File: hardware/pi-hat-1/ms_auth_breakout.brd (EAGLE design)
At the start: 66.8 x 29.2 mm, 20 parts, among them IC1 ULN2003AD

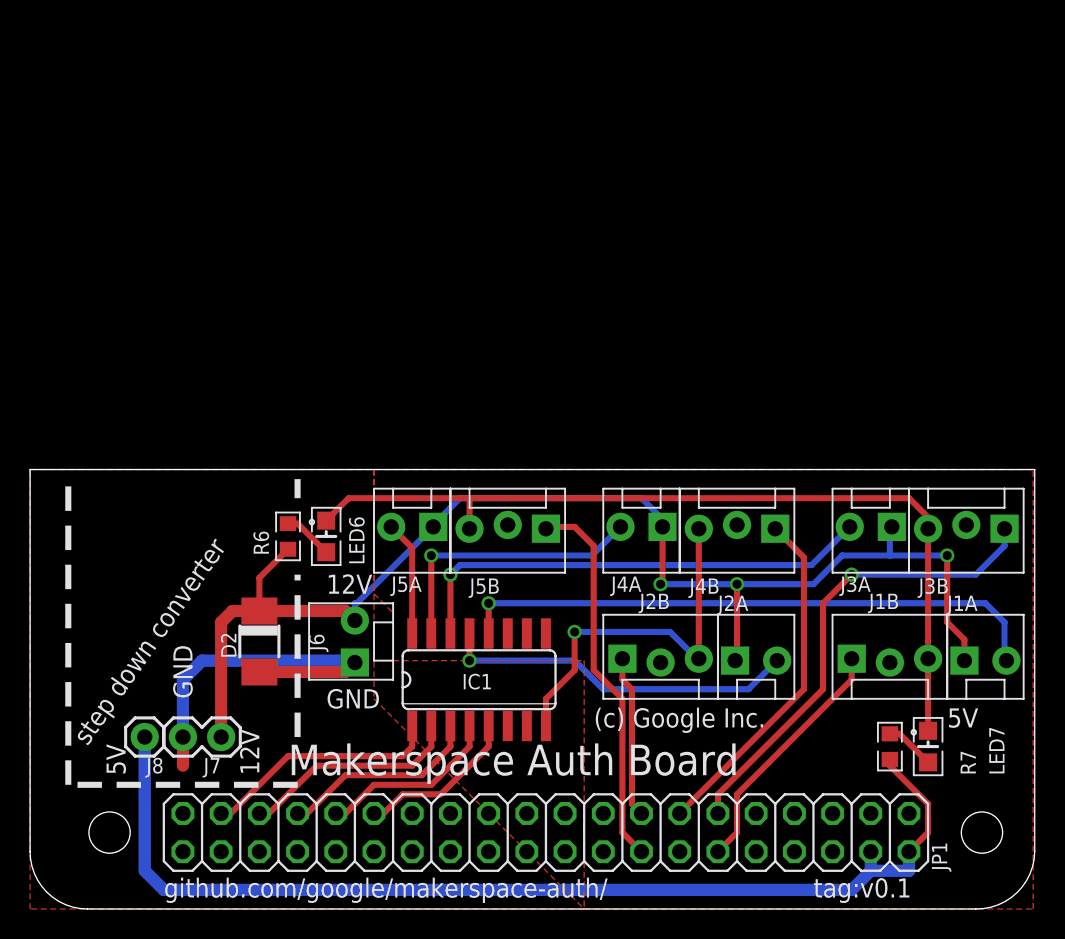
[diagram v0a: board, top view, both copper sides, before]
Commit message: Board v0.2 sent to fab.
This now has 5 button headers, a dedicated PowerSwitch Tail header, and
a dedicated buzzer.  Buck converter has been moved onboard, and we
connect to a 3rd mounting hole for stability.  Since there's room, add a
barrel jack.

This version includes the pin number on silkscreen next to each item.

The 5-pin locking part isn't yet upstreamed to SparkFun's library.
The vector logo in ms-logo.lbr isn't updated in the schematic.
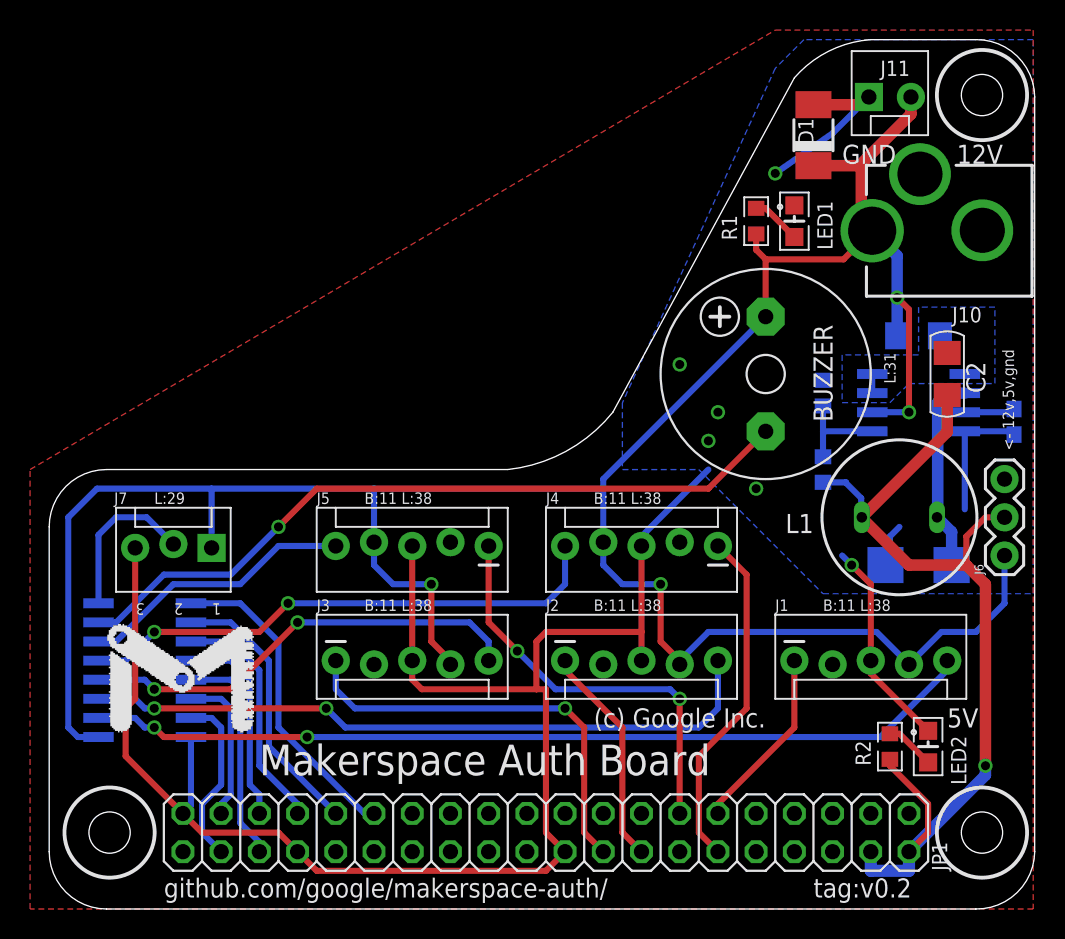
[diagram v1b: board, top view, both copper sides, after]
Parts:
- removed J1A, J2A, J3A, J4A, J5A: (no value), SparkFun-Connectors:MOLEX-1X2_LOCK
- removed J1B, J2B, J3B, J4B, J5B: (no value), SparkFun-Connectors:MOLEX-1X3_LOCK
- removed J8: (no value), SparkFun-Connectors:1X01
- removed LED6: LED, Tim-Pretty:CHIPLED_0805
- removed R6: (no value), Tim-Pretty:R0603
- added BUZZER: F/CM12P, buzzer:F/CM12P
- added C1: (no value), Tim-Pretty:C0603
- added C2: (no value), Tim-Pretty:C1206
- added D1: (no value), diode:DO-214AC
- added IC2: MC3X063AD, mc3x063:SO08
- added J1, J2, J3, J4, J5: (no value), SparkFun-Connectors:MOLEX-1X5_LOCK
- added J10: POWER_JACKPTH_LOCK, SparkFun-Connectors:POWER_JACK_PTH_LOCK
- added J11: (no value), SparkFun-Connectors:MOLEX-1X2_LOCK
- added L1: (no value), inductor-neosid:BS11
- added LED1: LED, Tim-Pretty:CHIPLED_0805
- added R1, R10, R11: (no value), Tim-Pretty:R0603
- added R12: (no value), Tim-Pretty:R1206
- added U$1: MS_LOGO, ms-logo:MS_LOGO
- D2: device diode:DO-214AC -> diode:SMB
- J6: device SparkFun-Connectors:MOLEX-1X2_LOCK -> SparkFun-Connectors:1X03
- J7: device SparkFun-Connectors:1X02 -> SparkFun-Connectors:MOLEX-1X3_LOCK
- moved D2 44.1 mm to (59.1, 22.9), flipped to the bottom, turned to 0 degrees
- moved J6 43.7 mm to (64.8, 23.5)
- moved IC1 22.2 mm to (7.62, 15.9), flipped to the bottom, turned to 270 degrees
- moved J7 12.7 mm to (12.1, 24.1)
- renumbered LED7 to LED2, R7 to R2
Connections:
- new net L6_LOGIC: IC1.2, JP1.31
- new net L7_LOGIC: IC1.1, JP1.29
- new net N$1: D2.C, IC2.2, L1.2
- new net N$2: BUZZER.-, IC1.15
- new net N$3: IC2.5, R10.2, R11.1
- new net N$4: IC1.16, J7.2
- new net N$5: IC2.1, IC2.7, IC2.8, R12.2
- new net N$8: C1.1, IC2.3
- net !L1: now also IC1.10, J1.5; no longer IC1.12, J1A.2
- net !L2: now also IC1.11, J2.5; no longer IC1.13, J2A.2
- net !L3: now also IC1.12, J3.5; no longer IC1.14, J3A.2
- net !L4: now also IC1.13, J4.5; no longer IC1.15, J4A.2
- net !L5: now also IC1.14, J5.5; no longer IC1.16, J5A.2
- net +12V: now also BUZZER.+, D1.C, IC1.9, IC2.6, J1.4, J10.PWR, J11.2, J2.4, J3.4, J4.4, J5.4, J6.1, R1.2, R12.1; no longer D2.C, J1A.1, J2A.1, J3A.1, J4A.1, J5A.1, J6.2, R6.2
- net +5V: now also C2.1, J6.2, L1.1, R10.1; no longer J8.1
- net B1_LOGIC: now also J1.1, JP1.11; no longer J1B.1, JP1.12
- net B2_LOGIC: now also J2.1, JP1.16; no longer J2B.1, JP1.15
- net B3_LOGIC: now also J3.1, JP1.18; no longer J3B.1, JP1.11
- net B4_LOGIC: now also J4.1, JP1.12; no longer J4B.1, JP1.13
- net B5_LOGIC: now also J5.1, JP1.13; no longer J5B.1, JP1.16
- net GND: now also C1.2, C2.2, D1.A, IC2.4, J1.3, J10.GND, J10.GNDBREAK, J11.1, J2.3, J3.3, J4.3, J5.3, J6.3, J7.3, LED1.C, R11.2; no longer IC1.6, IC1.7, J1B.3, J2B.3, J3B.3, J4B.3, J5B.3, J6.1, J7.2, LED6.C
- net L1_LOGIC: now also IC1.7, JP1.38; no longer IC1.5, JP1.29
- net L2_LOGIC: now also IC1.6, JP1.37; no longer IC1.4, JP1.31
- net L3_LOGIC: now also IC1.5, JP1.36; no longer IC1.3, JP1.33
- net L4_LOGIC: now also IC1.4; no longer IC1.2
- net L5_LOGIC: now also IC1.3, JP1.33; no longer IC1.1, JP1.37
- net N$11: now also LED1.A, R1.1; no longer LED6.A, R6.1
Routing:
- net +12V: track 85.9 -> 176.8 mm, vias 3 -> 4
- net N$2: track 0.00 -> 49.6 mm, vias 0 -> 1
- net GND: track 106.4 -> 144.1 mm, vias 1 -> 6
- net !L2: track 23.8 -> 45.7 mm, vias 1 -> 2
- net L7_LOGIC: track 0.00 -> 21.3 mm
- net !L1: track 39.6 -> 59.4 mm, vias 1 -> 2
- net L6_LOGIC: track 0.00 -> 18.2 mm
- net !L4: track 18.5 -> 35.7 mm, vias 1 -> 2
- net N$1: track 0.00 -> 13.3 mm
- net N$4: track 0.00 -> 10.7 mm
- net !L5: track 7.67 -> 18.4 mm
- net +5V: track 71.0 -> 62.5 mm, vias 0 -> 1
- net N$3: track 0.00 -> 6.66 mm
- net B1_LOGIC: track 16.5 -> 12.3 mm
- net B2_LOGIC: track 10.8 -> 14.8 mm
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- added copper zone on layer 16, net GND
- added copper zone on layer 16, net N$5
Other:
- board size 66.8 x 29.2 mm -> 65.5 x 57.8 mm
- board text added: "1"
- board text added: "2"
- board text added: "3"
- board text added: "<- 12v,5v,gnd"
- board text added: "B:11 L:38"
- board text added: "L:29"
- board text added: "L:31"
- board text added: "tag:v0.2"
- board text removed: "step down converter"
- board text removed: "tag:v0.1"

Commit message: Begin v0.3 of auth board
Improve 12V trace routing down the middle; swap to vector logo.
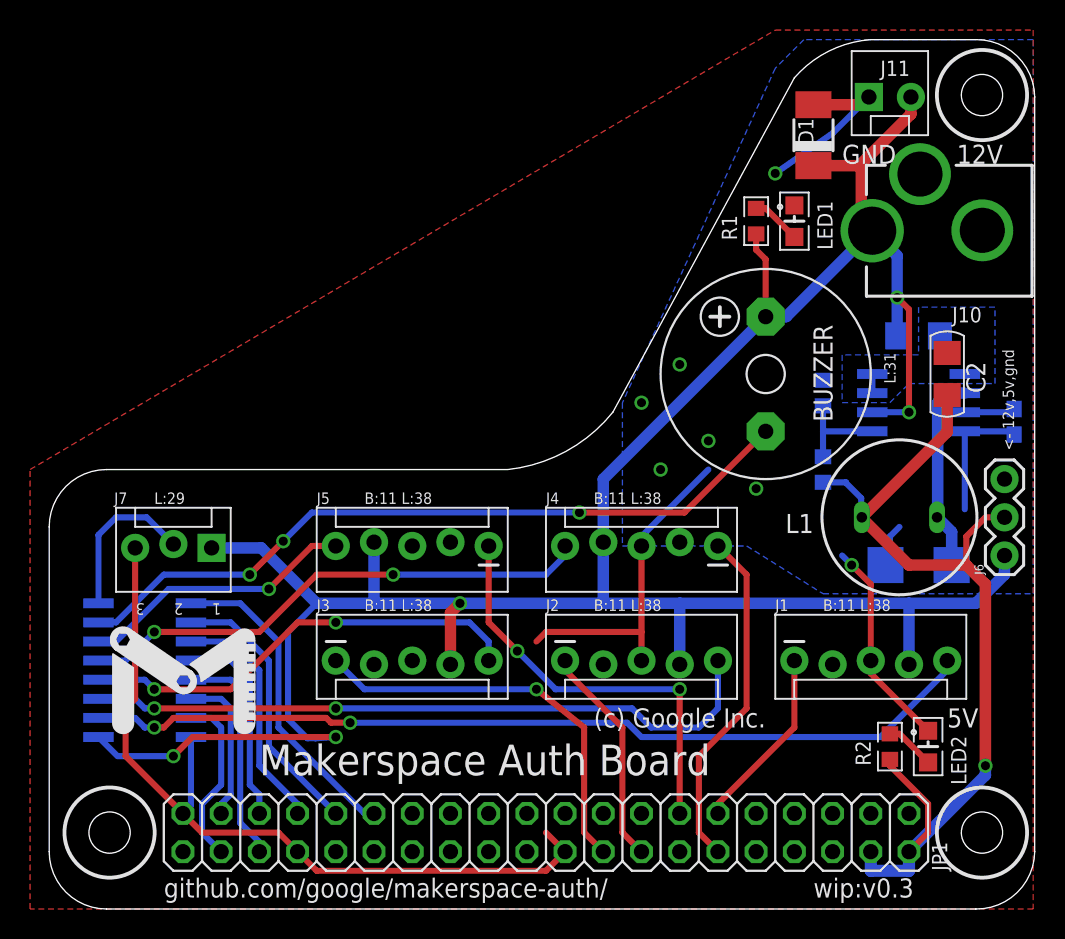
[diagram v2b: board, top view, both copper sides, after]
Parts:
- U$1: device ms-logo:MS_LOGO -> ms-logo:MS_LOGO_VECTOR
- moved U$1 6.35 mm to (5.08, 11.4)
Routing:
- net GND: track 144.1 -> 113.3 mm, vias 6 -> 7
- net +12V: track 176.8 -> 172.4 mm, vias 4 -> 5
- net B3_LOGIC: track 28.2 -> 27.0 mm
- net !L4: track 35.7 -> 34.5 mm
- net !L1: track 59.4 -> 59.9 mm
- net N$2: vias 1 -> 3
- net !L5: vias 0 -> 1
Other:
- board text added: "wip:v0.3"
- board text removed: "tag:v0.2"

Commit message: Getting ready to order pi-hat-1 v0.3
I re-routed this almost completely.  The area in the middle now makes a bit
more sense, and there's only one ground island that had to be reconnected.

* Switched back to buck module
* Found room for 6 button connectors again
* Added discrete RGB LED driver
* Added higher current output for inductive loads
  (ULN2003 maxes out at 500mA continuous, and I've popped a few trying
  solenoids without additional diodes)
* Pulldown resistors for the pins Robert discovered pulled high at boot
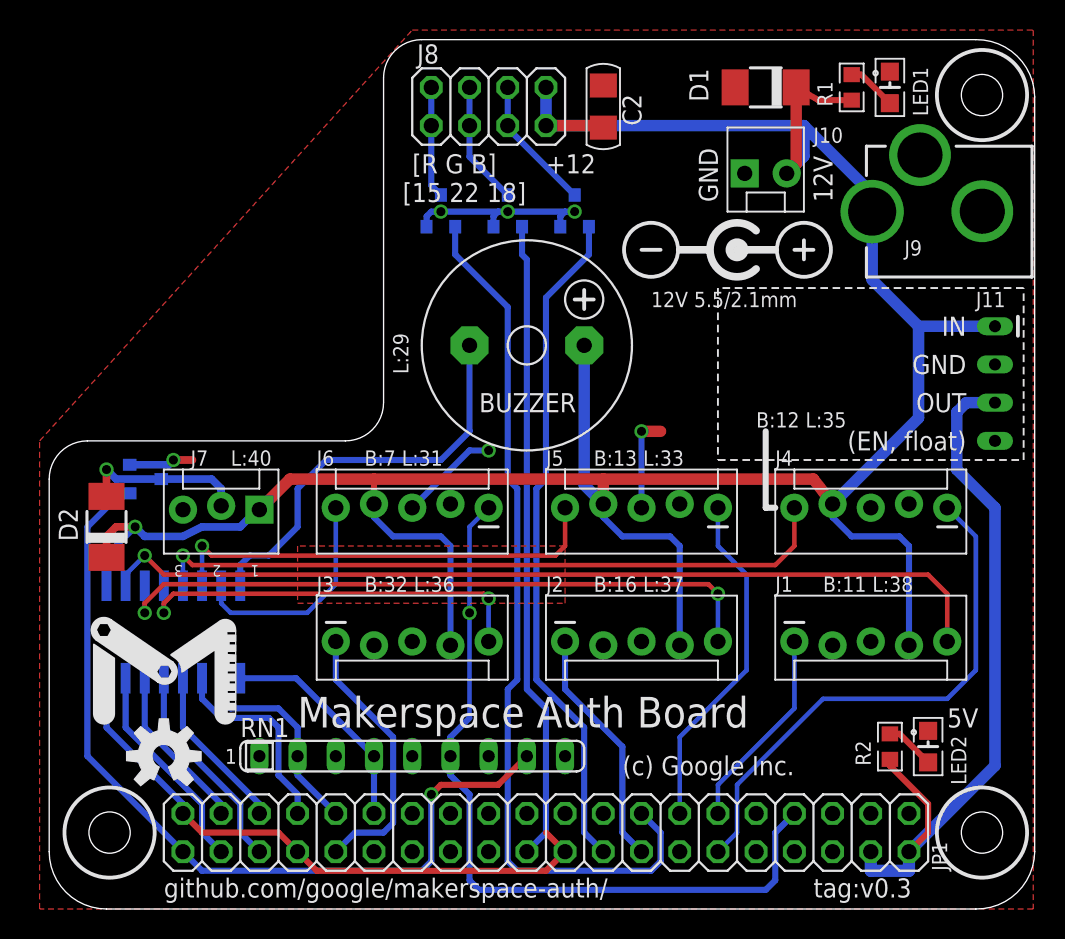
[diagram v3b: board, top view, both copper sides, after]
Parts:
- removed C1: (no value), Tim-Pretty:C0603
- removed IC2: MC3X063AD, mc3x063:SO08
- removed L1: (no value), inductor-neosid:BS11
- removed R10, R11: (no value), Tim-Pretty:R0603
- removed R12: (no value), Tim-Pretty:R1206
- added J8: (no value), pinhead:2X04
- added J9: POWER_JACKPTH_LOCK, SparkFun-Connectors:POWER_JACK_PTH_LOCK
- added LOGO1: OSHW-LOGOM, SparkFun-Aesthetics:OSHW-LOGO-M
- added Q1, Q2, Q3, Q4: DMN3023L, SparkFun-DiscreteSemi:SOT23-3
- added RN1: (no value), resistor-sil:SIL9
- C2: value (none) -> 47u
- D2: device diode:SMB -> diode:DO-214AC
- J10: value POWER_JACKPTH_LOCK -> (none); device SparkFun-Connectors:POWER_JACK_PTH_LOCK -> SparkFun-Connectors:MOLEX-1X2_LOCK
- J11: value (none) -> BUCK_MODULEHORIZONTAL; device SparkFun-Connectors:MOLEX-1X2_LOCK -> buck-module:BUCK_HORIZONTAL
- J6: device SparkFun-Connectors:1X03 -> SparkFun-Connectors:MOLEX-1X5_LOCK
- R1: value (none) -> 1k
- R2: value (none) -> 330
- moved D2 54.0 mm to (5.08, 25.4), flipped to the top, turned to 90 degrees
- moved J6 34.4 mm to (30.5, 26.7), turned to 180 degrees
- moved C2 29.0 mm to (38.1, 53.3)
- moved J10 22.5 mm to (47.6, 48.9), turned to 0 degrees
- moved J11 19.6 mm to (64.1, 36.2), turned to 180 degrees
- moved BUZZER 16.0 mm to (33.0, 37.5), turned to 0 degrees
- moved J4 15.5 mm to (61.0, 26.7)
- moved J5 15.5 mm to (45.7, 26.7)
- moved LED1 10.9 mm to (57.1, 54.6)
- moved R1 10.9 mm to (54.6, 54.6)
- moved D1 4.49 mm to (48.9, 54.6), turned to 180 degrees
- moved J7 4.07 mm to (15.2, 26.7)
- moved IC1 3.17 mm to (9.53, 18.4), turned to 0 degrees
- moved U$1 1.42 mm to (3.81, 12.1)
- moved J1 1.27 mm to (50.8, 17.8)
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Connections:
- removed net N$1: D2.C, IC2.2, L1.2
- removed net N$2: BUZZER.-, IC1.15
- removed net N$3: IC2.5, R10.2, R11.1
- removed net N$5: IC2.1, IC2.7, IC2.8, R12.2
- removed net N$8: C1.1, IC2.3
- new net !B: J8.5, J8.6, Q3.3
- new net !G: J8.3, J8.4, Q2.3
- new net !L6: IC1.15, J6.5
- new net !R: J8.1, J8.2, Q1.3
- new net B6_LOGIC: J6.1, JP1.7, RN1.6
- new net B_LOGIC: JP1.18, Q3.1
- new net G_LOGIC: JP1.22, Q2.1
- new net HC_LOGIC: JP1.40, Q4.1, RN1.8
- new net N$13: BUZZER.-, IC1.16
- new net R_LOGIC: JP1.15, Q1.1
- net +12V: now also C2.1, D2.C, J10.2, J11.IN, J6.4, J8.7, J8.8, J9.PWR; no longer IC2.6, J10.PWR, J11.2, J6.1, R12.1
- net +5V: now also J11.OUT; no longer C2.1, J6.2, L1.1, R10.1
- net B3_LOGIC: now also JP1.32; no longer JP1.18
- net GND: now also J10.1, J11.GND, J9.GND, J9.GNDBREAK, Q1.2, Q2.2, Q3.2, Q4.2, RN1.1, RN1.3, RN1.5, RN1.7; no longer C1.2, D2.A, IC2.4, J10.GND, J10.GNDBREAK, J11.1, R11.2
- net L6_LOGIC: now also RN1.2
- net L7_LOGIC: now also RN1.4
- net N$4: now also D2.A, Q4.3; no longer IC1.16
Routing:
- net R_LOGIC: track 0.00 -> 58.5 mm
- net HC_LOGIC: track 0.00 -> 57.1 mm, vias 0 -> 1
- net B6_LOGIC: track 0.00 -> 52.2 mm, vias 0 -> 1
- net N$2: track 49.6 -> 0.00 mm, vias 3 -> 0
- net B_LOGIC: track 0.00 -> 44.8 mm
- net G_LOGIC: track 0.00 -> 42.7 mm
- net GND: track 113.3 -> 70.6 mm, vias 7 -> 6
- net N$13: track 0.00 -> 27.5 mm
- net !L6: track 0.00 -> 14.9 mm
- net +5V: track 62.5 -> 48.2 mm, vias 1 -> 0
- net N$1: track 13.3 -> 0.00 mm
- net B4_LOGIC: track 23.0 -> 35.6 mm
- net +12V: track 172.4 -> 184.4 mm, vias 5 -> 1
- net !L4: track 34.5 -> 46.0 mm, vias 2 -> 1
- net !L5: track 18.4 -> 29.8 mm
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- added copper zone on layer 1, net N$1
- removed copper zone on layer 16, net GND
- removed copper zone on layer 16, net N$5
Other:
- outline, holes or cut-outs redrawn
- board text added: "(CSI bus)"
- board text added: "(HDMI)"
- board text added: "+12"
- board text added: "12V 5.5/2.1mm"
- board text added: "B:12 L:35"
- board text added: "B:13 L:33"
- board text added: "B:16 L:37"
- board text added: "B:32 L:36"
- board text added: "B:7 L:31"
- board text added: "J11"
- board text added: "L:40"
- board text added: "[15 22 18]"
- board text added: "[R G B]"
- board text added: "tag:v0.3"
- board text removed: "<- 12v,5v,gnd"
- board text removed: "L:31"
- board text removed: "wip:v0.3"
